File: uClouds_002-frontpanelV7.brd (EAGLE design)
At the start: 40.6 x 128.5 mm, 1 part

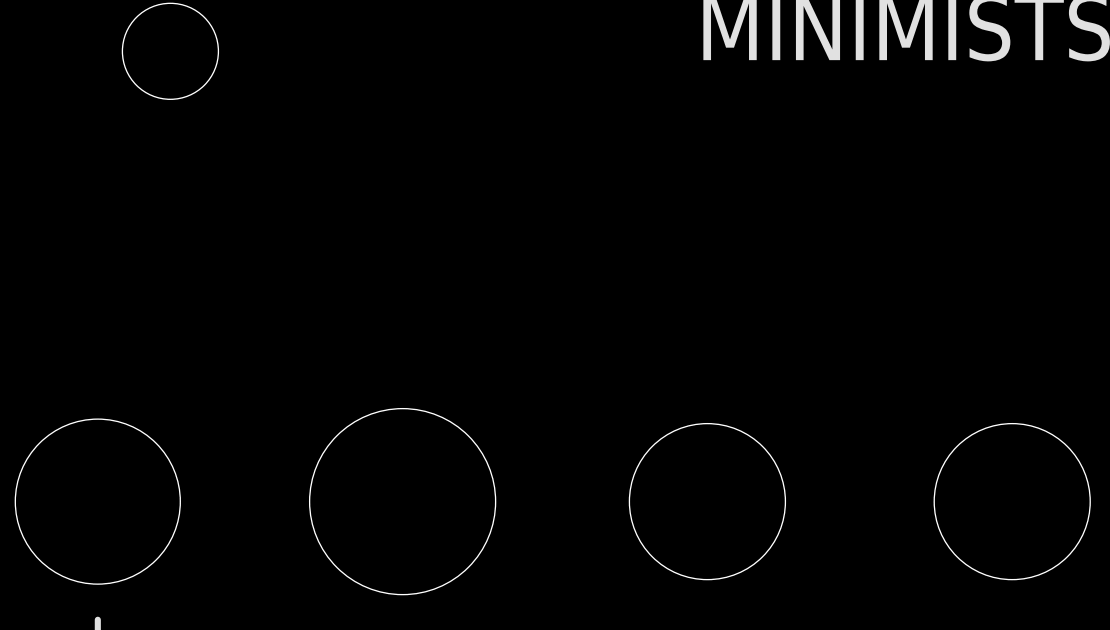
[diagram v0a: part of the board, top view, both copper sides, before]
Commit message: logo's en stopmask
- logo's weer uit Tstop gehaald.
- Gaten weer in Tstop gezet.
- Logos' in Top gemaakt.
- Logo's in tNames gemaakt.

Klaar volgens mij.
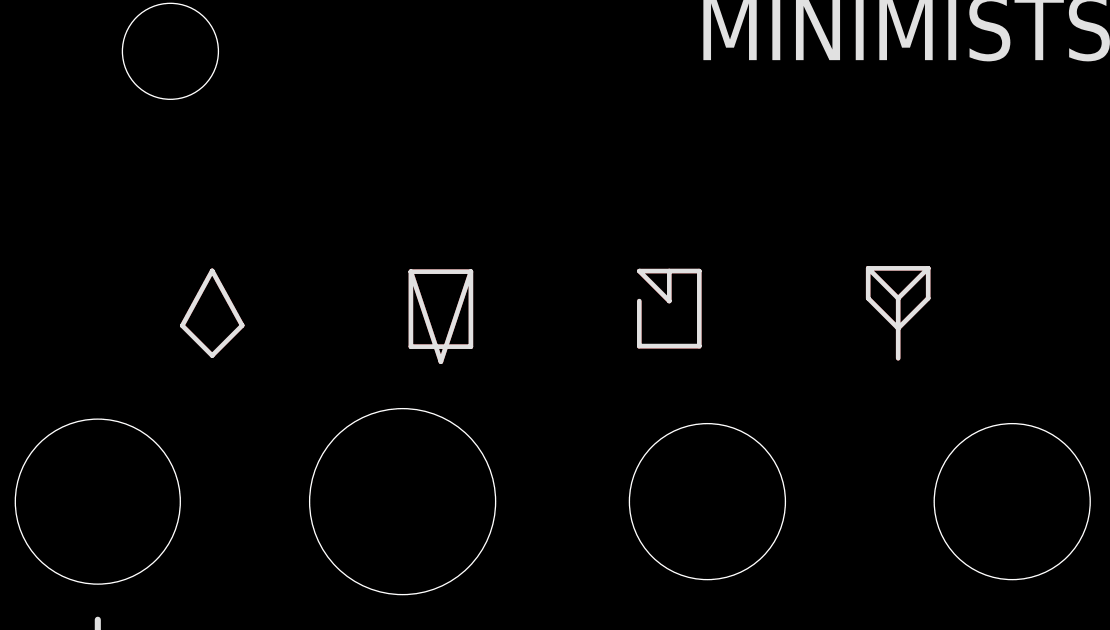
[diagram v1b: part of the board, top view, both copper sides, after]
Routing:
- net S$2: track 0.00 -> 15.3 mm
- net S$4: track 0.00 -> 11.7 mm
- net S$3: track 0.00 -> 10.4 mm
- net S$1: track 0.00 -> 6.98 mm
